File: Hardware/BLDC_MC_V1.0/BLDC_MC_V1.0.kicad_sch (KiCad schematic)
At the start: 0 parts

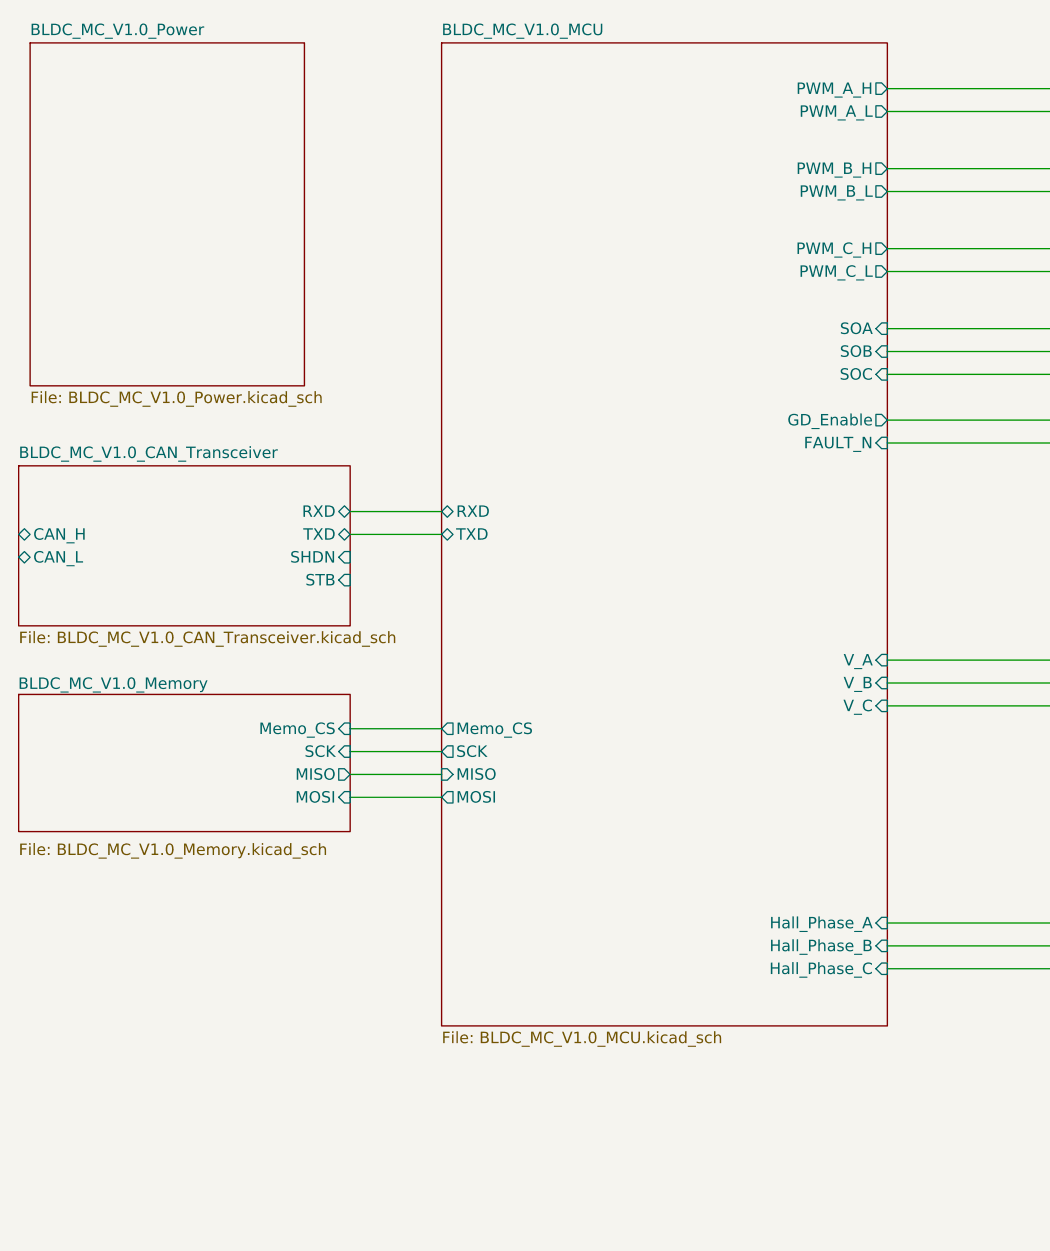
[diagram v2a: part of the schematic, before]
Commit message: Edit the controller sheet and CAN sheet to adjust the interface between them
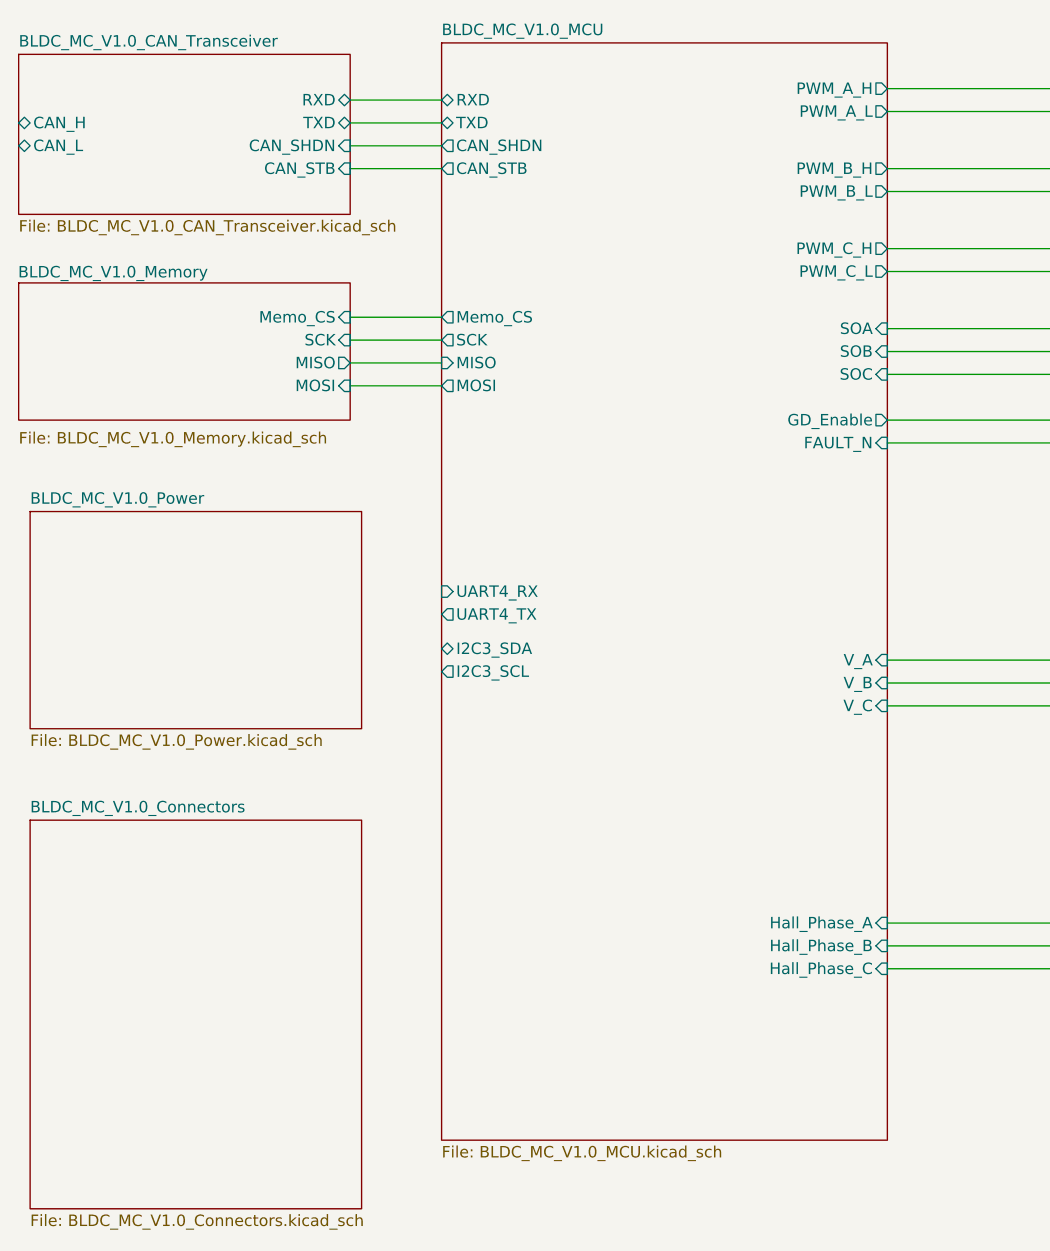
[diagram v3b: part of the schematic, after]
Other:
- added sheet BLDC_MC_V1.0_Connectors (BLDC_MC_V1.0_Connectors.kicad_sch)
- sheet BLDC_MC_V1.0_CAN_Transceiver ports: added CAN_SHDN, CAN_STB; removed SHDN, STB
- sheet BLDC_MC_V1.0_MCU ports: added CAN_SHDN, CAN_STB, I2C3_SCL, I2C3_SDA, UART4_RX, UART4_TX; removed none
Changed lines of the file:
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@@
 	(wire
 		(pts
-			(xy 77.47 123.19) (xy 87.63 123.19)
+			(xy 77.47 77.47) (xy 87.63 77.47)
 		)
 		(stroke
@@
 	(wire
 		(pts
-			(xy 77.47 128.27) (xy 87.63 128.27)
+			(xy 77.47 82.55) (xy 87.63 82.55)
 		)
 		(stroke
@@
 	(wire
 		(pts
-			(xy 77.47 125.73) (xy 87.63 125.73)
+			(xy 77.47 80.01) (xy 87.63 80.01)
 		)
 		(stroke
@@
 	(wire
 		(pts
-			(xy 77.47 96.52) (xy 87.63 96.52)
+			(xy 77.47 50.8) (xy 87.63 50.8)
 		)
 		(stroke
@@
 	(wire
 		(pts
+			(xy 77.47 55.88) (xy 87.63 55.88)
+		)
+		(stroke
+			(width 0)
+			(type default)
+		)
+	)
+	(wire
+		(pts
 			(xy 203.2 78.74) (xy 219.71 78.74)
 		)
@@
 	(wire
 		(pts
-			(xy 77.47 120.65) (xy 87.63 120.65)
-		)
-		(stroke
-			(width 0)
-			(type default)
-		)
-	)
-	(wire
-		(pts
-			(xy 77.47 99.06) (xy 87.63 99.06)
+			(xy 77.47 74.93) (xy 87.63 74.93)
+		)
+		(stroke
+			(width 0)
+			(type default)
+		)
+	)
+	(wire
+		(pts
+			(xy 77.47 58.42) (xy 87.63 58.42)
+		)
+		(stroke
+			(width 0)
+			(type default)
+		)
+	)
+	(wire
+		(pts
+			(xy 77.47 53.34) (xy 87.63 53.34)
 		)
 		(stroke
@@
 	)
 	(sheet
-		(at 40.64 91.44)
+		(at 40.64 45.72)
 		(size 36.83 17.78)
 		(exclude_from_sim no)
@@
 		)
 		(property "Sheetname" "BLDC_MC_V1.0_CAN_Transceiver"
-			(at 40.64 90.7284 0)
+			(at 40.64 45.0084 0)
 			(effects
 				(font
@@
 		)
 		(property "Sheetfile" "BLDC_MC_V1.0_CAN_Transceiver.kicad_sch"
-			(at 40.64 109.8046 0)
+			(at 40.64 64.0846 0)
 			(effects
 				(font
@@
 		)
 		(pin "CAN_L" bidirectional
-			(at 40.64 101.6 180)
+			(at 40.64 55.88 180)
 			(effects
 				(font
@@
 		)
 		(pin "CAN_H" bidirectional
-			(at 40.64 99.06 180)
+			(at 40.64 53.34 180)
 			(effects
 				(font
@@
 		)
 		(pin "RXD" bidirectional
-			(at 77.47 96.52 0)
+			(at 77.47 50.8 0)
 			(effects
 				(font
@@
 		)
 		(pin "TXD" bidirectional
-			(at 77.47 99.06 0)
-			(effects
-				(font
-					(size 1.27 1.27)
-				)
-				(justify right)
-			)
-		)
-		(pin "SHDN" input
-			(at 77.47 101.6 0)
-			(effects
-				(font
-					(size 1.27 1.27)
-				)
-				(justify right)
-			)
-		)
-		(pin "STB" input
-			(at 77.47 104.14 0)
+			(at 77.47 53.34 0)
+			(effects
+				(font
+					(size 1.27 1.27)
+				)
+				(justify right)
+			)
+		)
+		(pin "CAN_SHDN" input
+			(at 77.47 55.88 0)
+			(effects
+				(font
+					(size 1.27 1.27)
+				)
+				(justify right)
+			)
+		)
+		(pin "CAN_STB" input
+			(at 77.47 58.42 0)
 			(effects
 				(font
@@
 			(project "BLDC_MC_V1.0"
 				(path "/e34fda66-7244-4ac9-bbf7-3725f03e688f"
-					(page "4")
+					(page "7")
 				)
 			)
@@
 			(project "BLDC_MC_V1.0"
 				(path "/e34fda66-7244-4ac9-bbf7-3725f03e688f"
-					(page "7")
+					(page "4")
+				)
+			)
+		)
+	)
+	(sheet
+		(at 41.91 130.81)
+		(size 36.83 43.18)
+		(exclude_from_sim no)
+		(in_bom yes)
+		(on_board yes)
+		(dnp no)
+		(fields_autoplaced yes)
+		(stroke
+			(width 0.1524)
+			(type solid)
+		)
+		(fill
+			(color 255 255 194 1.0000)
+		)
+		(property "Sheetname" "BLDC_MC_V1.0_Connectors"
+			(at 41.91 130.0984 0)
+			(effects
+				(font
+					(size 1.27 1.27)
+				)
+				(justify left bottom)
+			)
+		)
+		(property "Sheetfile" "BLDC_MC_V1.0_Connectors.kicad_sch"
+			(at 41.91 174.5746 0)
+			(effects
+				(font
+					(size 1.27 1.27)
+				)
+				(justify left top)
+			)
+		)
+		(instances
+			(project "BLDC_MC_V1.0"
+				(path "/e34fda66-7244-4ac9-bbf7-3725f03e688f"
+					(page "10")
 				)
 			)
@@
 			(project "BLDC_MC_V1.0"
 				(path "/e34fda66-7244-4ac9-bbf7-3725f03e688f"
-					(page "6")
+					(page "5")
 				)
 			)
@@
 	(sheet
 		(at 87.63 44.45)
-		(size 49.53 109.22)
+		(size 49.53 121.92)
 		(exclude_from_sim no)
 		(in_bom yes)
@@
 		)
 		(property "Sheetfile" "BLDC_MC_V1.0_MCU.kicad_sch"
-			(at 87.63 154.2546 0)
+			(at 87.63 166.9546 0)
 			(effects
 				(font
@@
 		)
 		(pin "TXD" bidirectional
-			(at 87.63 99.06 180)
+			(at 87.63 53.34 180)
 			(effects
 				(font
@@
 		)
 		(pin "RXD" bidirectional
-			(at 87.63 96.52 180)
+			(at 87.63 50.8 180)
 			(effects
 				(font
@@
 		)
 		(pin "SCK" output
-			(at 87.63 123.19 180)
+			(at 87.63 77.47 180)
 			(effects
 				(font
@@
 		)
 		(pin "MISO" input
-			(at 87.63 125.73 180)
+			(at 87.63 80.01 180)
 			(effects
 				(font
@@
 		)
 		(pin "MOSI" output
-			(at 87.63 128.27 180)
+			(at 87.63 82.55 180)
 			(effects
 				(font
@@
 		)
 		(pin "Memo_CS" output
-			(at 87.63 120.65 180)
+			(at 87.63 74.93 180)
 			(effects
 				(font
@@
 				)
 				(justify right)
+			)
+		)
+		(pin "CAN_STB" output
+			(at 87.63 58.42 180)
+			(effects
+				(font
+					(size 1.27 1.27)
+				)
+				(justify left)
+			)
+		)
+		(pin "CAN_SHDN" output
+			(at 87.63 55.88 180)
+			(effects
+				(font
+					(size 1.27 1.27)
+				)
+				(justify left)
+			)
+		)
+		(pin "UART4_RX" input
+			(at 87.63 105.41 180)
+			(effects
+				(font
+					(size 1.27 1.27)
+				)
+				(justify left)
+			)
+		)
+		(pin "I2C3_SCL" output
+			(at 87.63 114.3 180)
+			(effects
+				(font
+					(size 1.27 1.27)
+				)
+				(justify left)
+			)
+		)
+		(pin "UART4_TX" output
+			(at 87.63 107.95 180)
+			(effects
+				(font
+					(size 1.27 1.27)
+				)
+				(justify left)
+			)
+		)
+		(pin "I2C3_SDA" bidirectional
+			(at 87.63 111.76 180)
+			(effects
+				(font
+					(size 1.27 1.27)
+				)
+				(justify left)
 			)
 		)
@@
 	)
 	(sheet
-		(at 40.64 116.84)
+		(at 40.64 71.12)
 		(size 36.83 15.24)
 		(exclude_from_sim no)
@@
 		)
 		(property "Sheetname" "BLDC_MC_V1.0_Memory"
-			(at 40.5743 116.3801 0)
+			(at 40.5743 70.6601 0)
 			(effects
 				(font
@@
 		)
 		(property "Sheetfile" "BLDC_MC_V1.0_Memory.kicad_sch"
-			(at 40.64 133.35 0)
+			(at 40.64 87.63 0)
 			(effects
 				(font
@@
 		)
 		(pin "MOSI" input
-			(at 77.47 128.27 0)
+			(at 77.47 82.55 0)
 			(effects
 				(font
@@
 		)
 		(pin "SCK" input
-			(at 77.47 123.19 0)
+			(at 77.47 77.47 0)
 			(effects
 				(font
@@
 		)
 		(pin "Memo_CS" input
-			(at 77.47 120.65 0)
+			(at 77.47 74.93 0)
 			(effects
 				(font
@@
 		)
 		(pin "MISO" output
-			(at 77.47 125.73 0)
+			(at 77.47 80.01 0)
 			(effects
 				(font
@@
 			(project "BLDC_MC_V1.0"
 				(path "/e34fda66-7244-4ac9-bbf7-3725f03e688f"
-					(page "5")
+					(page "6")
 				)
 			)
@@
 	)
 	(sheet
-		(at 41.91 44.45)
-		(size 30.48 38.1)
+		(at 41.91 96.52)
+		(size 36.83 24.13)
 		(exclude_from_sim no)
 		(in_bom yes)
@@
 		)
 		(property "Sheetname" "BLDC_MC_V1.0_Power"
-			(at 41.91 43.7384 0)
+			(at 41.91 95.8084 0)
 			(effects
 				(font
@@
 		)
 		(property "Sheetfile" "BLDC_MC_V1.0_Power.kicad_sch"
-			(at 41.91 83.1346 0)
-			(effects
-				(font
+			(at 41.91 121.2346 0)
+			(effects
+				(font

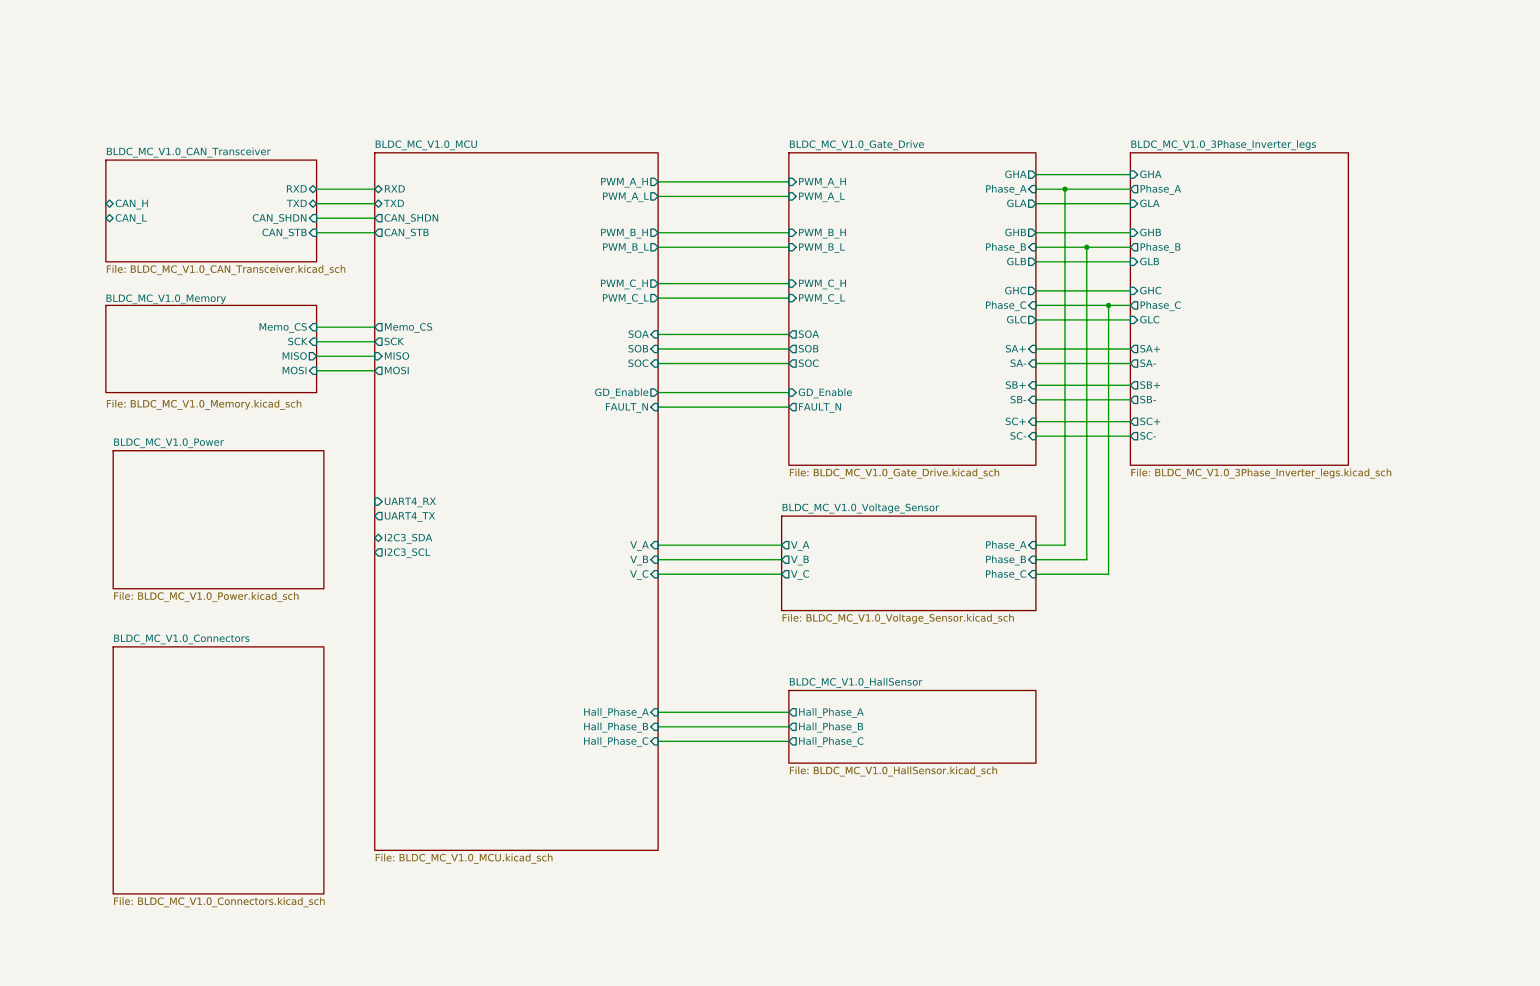
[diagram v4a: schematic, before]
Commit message: Adjust the connections between sheets
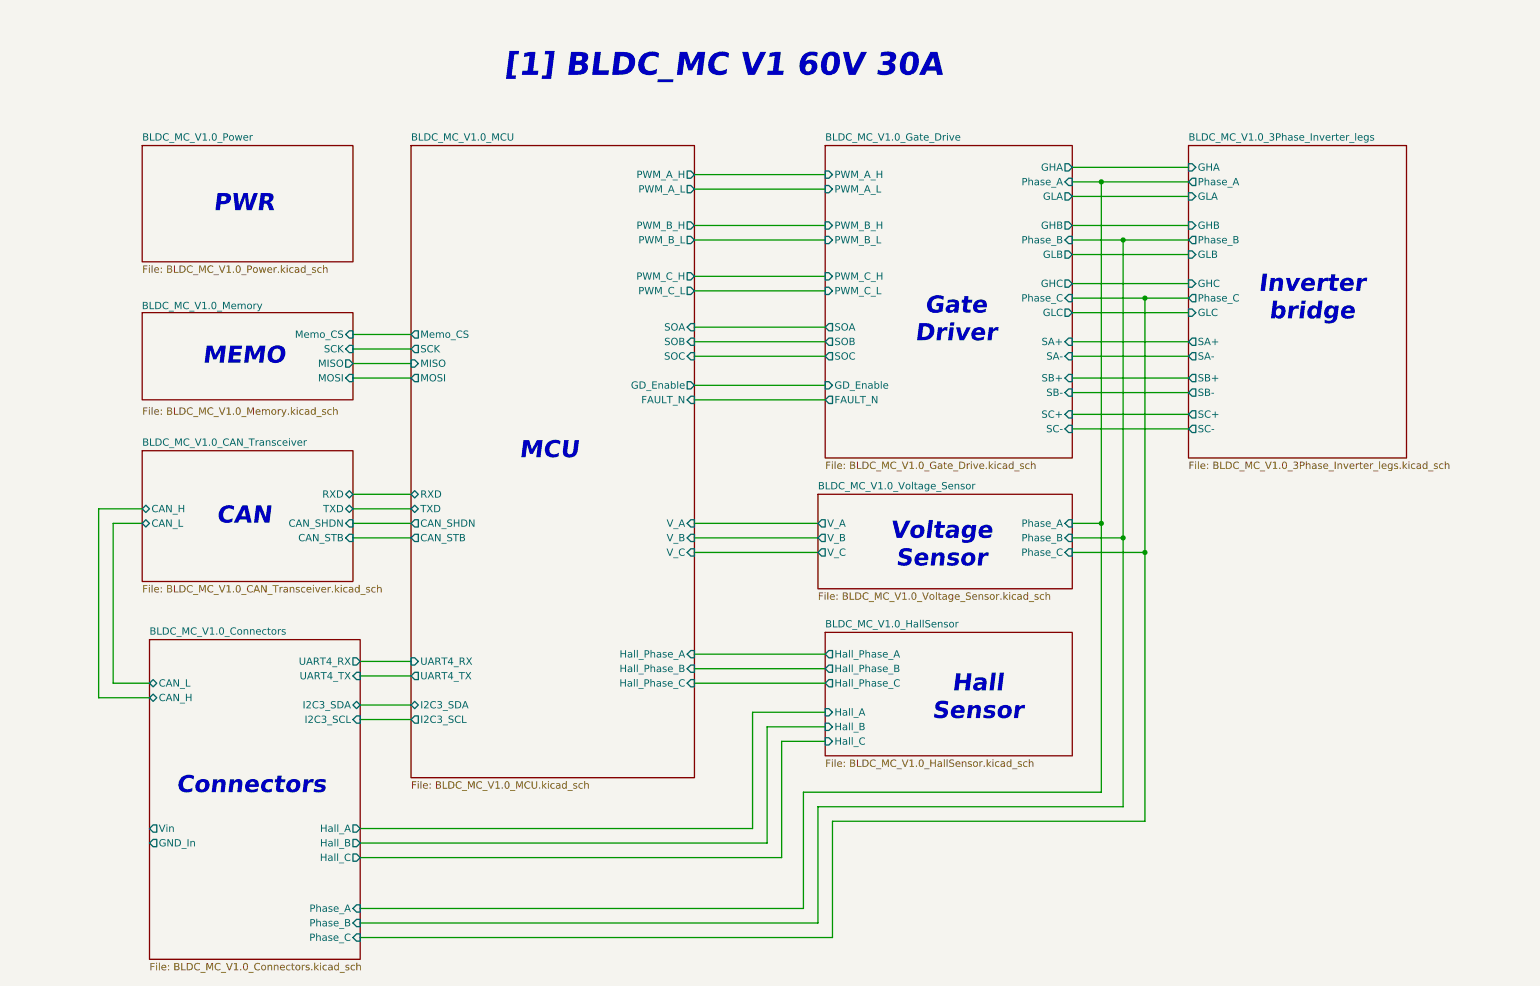
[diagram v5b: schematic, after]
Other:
- sheet BLDC_MC_V1.0_Connectors ports: added CAN_H, CAN_L, GND_In, Hall_A, Hall_B, Hall_C, I2C3_SCL, I2C3_SDA, Phase_A, Phase_B, Phase_C, UART4_RX, UART4_TX, Vin; removed none
- sheet BLDC_MC_V1.0_HallSensor ports: added Hall_A, Hall_B, Hall_C; removed none
- note added: "CAN"
- note added: "Connectors"
- note added: "Gate Driver"
- note added: "Hall Sensor"
- note added: "Inverter bridge"
- note added: "MCU"
- note added: "MEMO"
- note added: "PWR"
- note added: "Voltage Sensor"
- note added: "[1] BLDC_MC V1 60V 30A"

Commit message: Solve all errors and wornings in project
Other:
- sheet BLDC_MC_V1.0_Connectors ports: added Vin_DC; removed Vin
- sheet BLDC_MC_V1.0_Power ports: added GND_In, Vin_DC; removed none
